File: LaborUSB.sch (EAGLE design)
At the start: 8 parts

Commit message: Added iPhone charge capabilty, Component Names
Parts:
- added LOGO1: OSHW-LOGOM, SparkFun-Aesthetics:OSHW-LOGOM
- added R1: 43K, resistor:R-EU_R0805
- added R2: 75K, resistor:R-EU_R0805
- added R3, R4: 51K, resistor:R-EU_R0805
- renumbered U$1 to USB1, U$2 to USB2, U$3 to USB3, U$4 to USB4
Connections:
- new net D+: R2.1, R4.2, USB1.D+, USB2.D+, USB3.D+, USB4.D+
- new net D-: R1.1, R3.2, USB1.D-, USB2.D-, USB3.D-, USB4.D-
- net GND: now also R3.1, R4.1
- net VBUS: now also R1.2, R2.2
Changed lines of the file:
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@@
 <part name="J3" library="LaborUSB" deviceset="BANANA" device=""/>
 <part name="J4" library="LaborUSB" deviceset="BANANA" device=""/>
-<part name="U$1" library="LaborUSB" deviceset="USB+SHIELD" device=""/>
-<part name="U$2" library="LaborUSB" deviceset="USB+SHIELD" device=""/>
-<part name="U$3" library="LaborUSB" deviceset="USB+SHIELD" device=""/>
-<part name="U$4" library="LaborUSB" deviceset="USB+SHIELD" device=""/>
+<part name="USB1" library="LaborUSB" deviceset="USB+SHIELD" device=""/>
+<part name="USB2" library="LaborUSB" deviceset="USB+SHIELD" device=""/>
+<part name="USB3" library="LaborUSB" deviceset="USB+SHIELD" device=""/>
+<part name="USB4" library="LaborUSB" deviceset="USB+SHIELD" device=""/>
+<part name="R1" library="resistor" deviceset="R-EU_" device="R0805" value="43K"/>
+<part name="R2" library="resistor" deviceset="R-EU_" device="R0805" value="75K"/>
+<part name="R3" library="resistor" deviceset="R-EU_" device="R0805" value="51K"/>
+<part name="R4" library="resistor" deviceset="R-EU_" device="R0805" value="51K"/>
+<part name="LOGO1" library="SparkFun-Aesthetics" deviceset="OSHW-LOGO" device="M"/>
 </parts>
 <sheets>
@@
 <instance part="J3" gate="G$1" x="40.64" y="144.78" rot="R270"/>
 <instance part="J4" gate="G$1" x="50.8" y="144.78" rot="R270"/>
-<instance part="U$1" gate="G$1" x="30.48" y="162.56" rot="R90"/>
-<instance part="U$2" gate="G$1" x="10.16" y="162.56" rot="R90"/>
-<instance part="U$3" gate="G$1" x="2.54" y="147.32" rot="R270"/>
-<instance part="U$4" gate="G$1" x="22.86" y="147.32" rot="R270"/>
+<instance part="USB1" gate="G$1" x="30.48" y="162.56" rot="R90"/>
+<instance part="USB2" gate="G$1" x="10.16" y="162.56" rot="R90"/>
+<instance part="USB3" gate="G$1" x="2.54" y="147.32" rot="R270"/>
+<instance part="USB4" gate="G$1" x="22.86" y="147.32" rot="R270"/>
+<instance part="R1" gate="G$1" x="58.42" y="165.1" rot="R90"/>
+<instance part="R2" gate="G$1" x="66.04" y="165.1" rot="R90"/>
+<instance part="R3" gate="G$1" x="58.42" y="144.78" rot="R90"/>
+<instance part="R4" gate="G$1" x="66.04" y="144.78" rot="R90"/>
+<instance part="LOGO1" gate="G$1" x="5.08" y="182.88"/>
 </instances>
 <busses>
-<bus name="VBUS,GND">
+<bus name="VBUS,GND,D+,D-">
 <segment>
-<wire x1="-2.54" y1="154.94" x2="53.34" y2="154.94" width="0.762" layer="92"/>
+<wire x1="-2.54" y1="154.94" x2="73.66" y2="154.94" width="0.762" layer="92"/>
 </segment>
 </bus>
@@
 </segment>
 <segment>
-<pinref part="U$2" gate="G$1" pin="GND"/>
+<pinref part="USB2" gate="G$1" pin="GND"/>
 <wire x1="10.16" y1="160.02" x2="10.16" y2="154.94" width="0.1524" layer="91"/>
 </segment>
 <segment>
-<pinref part="U$1" gate="G$1" pin="GND"/>
+<pinref part="USB1" gate="G$1" pin="GND"/>
 <wire x1="30.48" y1="160.02" x2="30.48" y2="154.94" width="0.1524" layer="91"/>
 </segment>
 <segment>
-<pinref part="U$4" gate="G$1" pin="GND"/>
+<pinref part="USB4" gate="G$1" pin="GND"/>
 <wire x1="22.86" y1="149.86" x2="22.86" y2="154.94" width="0.1524" layer="91"/>
 </segment>
 <segment>
-<pinref part="U$3" gate="G$1" pin="GND"/>
+<pinref part="USB3" gate="G$1" pin="GND"/>
 <wire x1="2.54" y1="149.86" x2="2.54" y2="154.94" width="0.1524" layer="91"/>
+</segment>
+<segment>
+<wire x1="71.12" y1="154.94" x2="71.12" y2="139.7" width="0.1524" layer="91"/>
+<pinref part="R3" gate="G$1" pin="1"/>
+<pinref part="R4" gate="G$1" pin="1"/>
+<wire x1="58.42" y1="139.7" x2="66.04" y2="139.7" width="0.1524" layer="91"/>
+<wire x1="66.04" y1="139.7" x2="71.12" y2="139.7" width="0.1524" layer="91"/>
+<junction x="66.04" y="139.7"/>
 </segment>
 </net>
@@
 </segment>
 <segment>
-<pinref part="U$2" gate="G$1" pin="VBUS"/>
+<pinref part="USB2" gate="G$1" pin="VBUS"/>
 <wire x1="7.62" y1="160.02" x2="7.62" y2="154.94" width="0.1524" layer="91"/>
 </segment>
 <segment>
-<pinref part="U$1" gate="G$1" pin="VBUS"/>
+<pinref part="USB1" gate="G$1" pin="VBUS"/>
 <wire x1="27.94" y1="160.02" x2="27.94" y2="154.94" width="0.1524" layer="91"/>
 </segment>
 <segment>
-<pinref part="U$4" gate="G$1" pin="VBUS"/>
+<pinref part="USB4" gate="G$1" pin="VBUS"/>
 <wire x1="25.4" y1="149.86" x2="25.4" y2="154.94" width="0.1524" layer="91"/>
 </segment>
 <segment>
-<pinref part="U$3" gate="G$1" pin="VBUS"/>
+<pinref part="USB3" gate="G$1" pin="VBUS"/>
 <wire x1="5.08" y1="149.86" x2="5.08" y2="154.94" width="0.1524" layer="91"/>
 </segment>
+<segment>
+<wire x1="71.12" y1="154.94" x2="71.12" y2="170.18" width="0.1524" layer="91"/>
+<pinref part="R1" gate="G$1" pin="2"/>
+<pinref part="R2" gate="G$1" pin="2"/>
+<wire x1="58.42" y1="170.18" x2="66.04" y2="170.18" width="0.1524" layer="91"/>
+<wire x1="66.04" y1="170.18" x2="71.12" y2="170.18" width="0.1524" layer="91"/>
+<junction x="66.04" y="170.18"/>
+</segment>
 </net>
+<net name="D+" class="0">
+<segment>
+<pinref part="USB2" gate="G$1" pin="D+"/>
+<wire x1="2.54" y1="160.02" x2="2.54" y2="154.94" width="0.1524" layer="91"/>
+</segment>
+<segment>
+<pinref part="USB1" gate="G$1" pin="D+"/>
+<wire x1="22.86" y1="160.02" x2="22.86" y2="154.94" width="0.1524" layer="91"/>
+</segment>
+<segment>
+<pinref part="USB3" gate="G$1" pin="D+"/>
+<wire x1="10.16" y1="149.86" x2="10.16" y2="154.94" width="0.1524" layer="91"/>
+</segment>
+<segment>
+<pinref part="USB4" gate="G$1" pin="D+"/>
+<wire x1="30.48" y1="149.86" x2="30.48" y2="154.94" width="0.1524" layer="91"/>
+</segment>
+<segment>
+<pinref part="R2" gate="G$1" pin="1"/>
+<wire x1="66.04" y1="160.02" x2="66.04" y2="154.94" width="0.1524" layer="91"/>
+</segment>
+<segment>
+<pinref part="R4" gate="G$1" pin="2"/>
+<wire x1="66.04" y1="149.86" x2="66.04" y2="154.94" width="0.1524" layer="91"/>
+</segment>
+</net>
+<net name="D-" class="0">
+<segment>
+<pinref part="USB2" gate="G$1" pin="D-"/>
+<wire x1="5.08" y1="160.02" x2="5.08" y2="154.94" width="0.1524" layer="91"/>
+</segment>
+<segment>
+<pinref part="USB1" gate="G$1" pin="D-"/>
+<wire x1="25.4" y1="160.02" x2="25.4" y2="154.94" width="0.1524" layer="91"/>
+</segment>
+<segment>
+<pinref part="USB3" gate="G$1" pin="D-"/>
+<wire x1="7.62" y1="149.86" x2="7.62" y2="154.94" width="0.1524" layer="91"/>
+</segment>
+<segment>
+<pinref part="USB4" gate="G$1" pin="D-"/>
+<wire x1="27.94" y1="149.86" x2="27.94" y2="154.94" width="0.1524" layer="91"/>
+</segment>
+<segment>
+<pinref part="R1" gate="G$1" pin="1"/>
+<wire x1="58.42" y1="160.02" x2="58.42" y2="154.94" width="0.1524" layer="91"/>
+</segment>
+<segment>
+<pinref part="R3" gate="G$1" pin="2"/>
+<wire x1="58.42" y1="149.86" x2="58.42" y2="154.94" width="0.1524" layer="91"/>
+</segment>
+</net>

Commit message: First prototype order
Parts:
- renumbered J1 to GND
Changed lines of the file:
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@@
 </classes>
 <parts>
-<part name="J1" library="LaborUSB" deviceset="BANANA" device=""/>
+<part name="GND" library="LaborUSB" deviceset="BANANA" device=""/>
 <part name="J2" library="LaborUSB" deviceset="BANANA" device=""/>
 <part name="J3" library="LaborUSB" deviceset="BANANA" device=""/>
@@
 </plain>
 <instances>
-<instance part="J1" gate="G$1" x="40.64" y="165.1" rot="R90"/>
+<instance part="GND" gate="G$1" x="40.64" y="165.1" rot="R90"/>
 <instance part="J2" gate="G$1" x="50.8" y="165.1" rot="R90"/>
 <instance part="J3" gate="G$1" x="40.64" y="144.78" rot="R270"/>
@@
 <segment>
 <wire x1="40.64" y1="162.56" x2="40.64" y2="154.94" width="0.1524" layer="91"/>
-<pinref part="J1" gate="G$1" pin="1"/>
+<pinref part="GND" gate="G$1" pin="1"/>
 </segment>
 <segment>

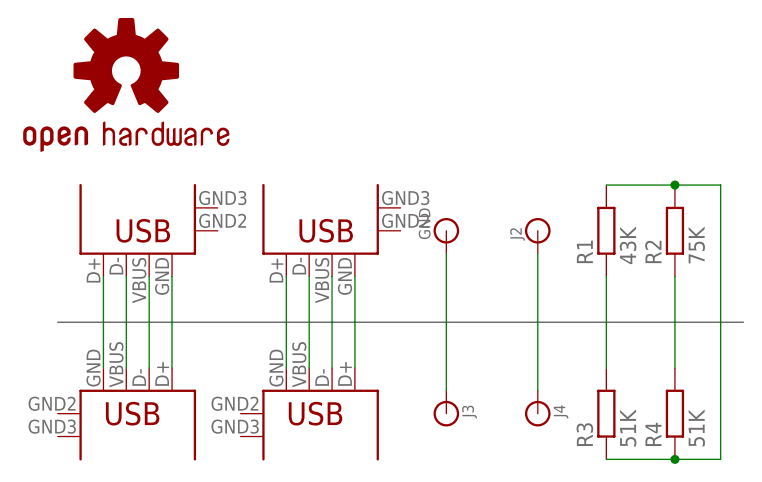
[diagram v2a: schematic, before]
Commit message: Fix in thermals on Banana Plug
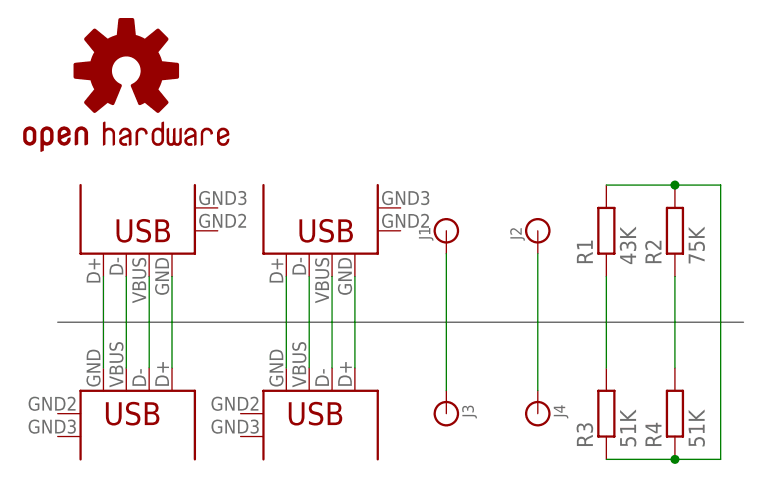
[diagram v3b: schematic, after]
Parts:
- renumbered GND to J1
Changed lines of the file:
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@@
 </classes>
 <parts>
-<part name="GND" library="LaborUSB" deviceset="BANANA" device=""/>
-<part name="J2" library="LaborUSB" deviceset="BANANA" device=""/>
-<part name="J3" library="LaborUSB" deviceset="BANANA" device=""/>
-<part name="J4" library="LaborUSB" deviceset="BANANA" device=""/>
 <part name="USB1" library="LaborUSB" deviceset="USB+SHIELD" device=""/>
 <part name="USB2" library="LaborUSB" deviceset="USB+SHIELD" device=""/>
@@
 <part name="R4" library="resistor" deviceset="R-EU_" device="R0805" value="51K"/>
 <part name="LOGO1" library="SparkFun-Aesthetics" deviceset="OSHW-LOGO" device="M"/>
+<part name="J1" library="LaborUSB" deviceset="BANANA" device=""/>
+<part name="J2" library="LaborUSB" deviceset="BANANA" device=""/>
+<part name="J3" library="LaborUSB" deviceset="BANANA" device=""/>
+<part name="J4" library="LaborUSB" deviceset="BANANA" device=""/>
 </parts>
 <sheets>
@@
 </plain>
 <instances>
-<instance part="GND" gate="G$1" x="40.64" y="165.1" rot="R90"/>
-<instance part="J2" gate="G$1" x="50.8" y="165.1" rot="R90"/>
-<instance part="J3" gate="G$1" x="40.64" y="144.78" rot="R270"/>
-<instance part="J4" gate="G$1" x="50.8" y="144.78" rot="R270"/>
 <instance part="USB1" gate="G$1" x="30.48" y="162.56" rot="R90"/>
 <instance part="USB2" gate="G$1" x="10.16" y="162.56" rot="R90"/>
@@
 <instance part="R4" gate="G$1" x="66.04" y="144.78" rot="R90"/>
 <instance part="LOGO1" gate="G$1" x="5.08" y="182.88"/>
+<instance part="J1" gate="G$1" x="40.64" y="165.1" rot="R90"/>
+<instance part="J2" gate="G$1" x="50.8" y="165.1" rot="R90"/>
+<instance part="J3" gate="G$1" x="40.64" y="144.78" rot="R270"/>
+<instance part="J4" gate="G$1" x="50.8" y="144.78" rot="R270"/>
 </instances>
 <busses>
@@
 <segment>
 <wire x1="40.64" y1="162.56" x2="40.64" y2="154.94" width="0.1524" layer="91"/>
-<pinref part="GND" gate="G$1" pin="1"/>
+<pinref part="J1" gate="G$1" pin="1"/>
 </segment>
 <segment>
